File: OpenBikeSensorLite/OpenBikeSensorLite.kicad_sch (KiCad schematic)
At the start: 6 parts, among them J1 Sensor A, J2 Sensor B, J3 I^{2}C, J4 Button, U1 ESP32-DEVKIT-32C

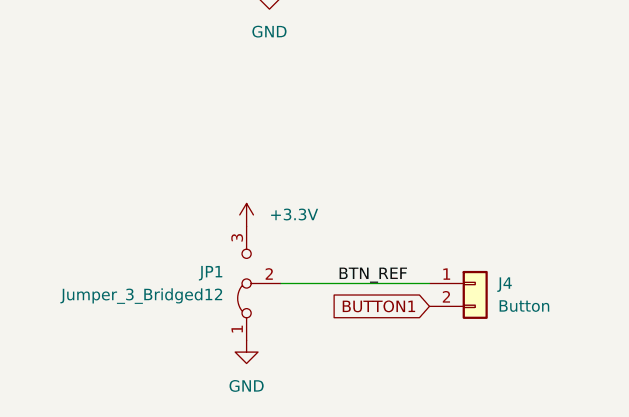
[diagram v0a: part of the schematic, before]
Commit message: fix issue: because D2 also has the LED connected to it we can never use "active low" on that pin (the LED is stronger than the internal pullup). Therefore we can connect 3V3 to the other leg of the button.
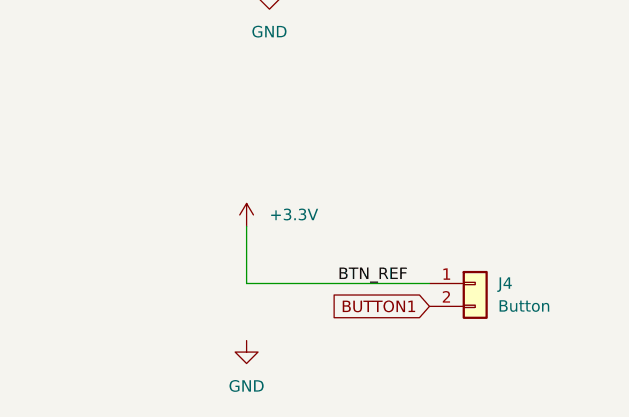
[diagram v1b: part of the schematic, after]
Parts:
- removed JP1: Jumper_3_Bridged12, Jumper:SolderJumper-3_P1.3mm_Bridged12_Pad1.0x1.5mm, symbol Jumper:Jumper_3_Bridged12
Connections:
- net BTN_REF is gone; now on net +3V3: J4.1 (Pin_1)
